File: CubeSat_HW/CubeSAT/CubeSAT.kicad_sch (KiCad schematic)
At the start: 12 parts, among them J1 Conn_02x06_Odd_Even, J2 Conn_02x04_Odd_Even, J4 Conn_01x08_Pin, J5 Conn_01x06_Pin

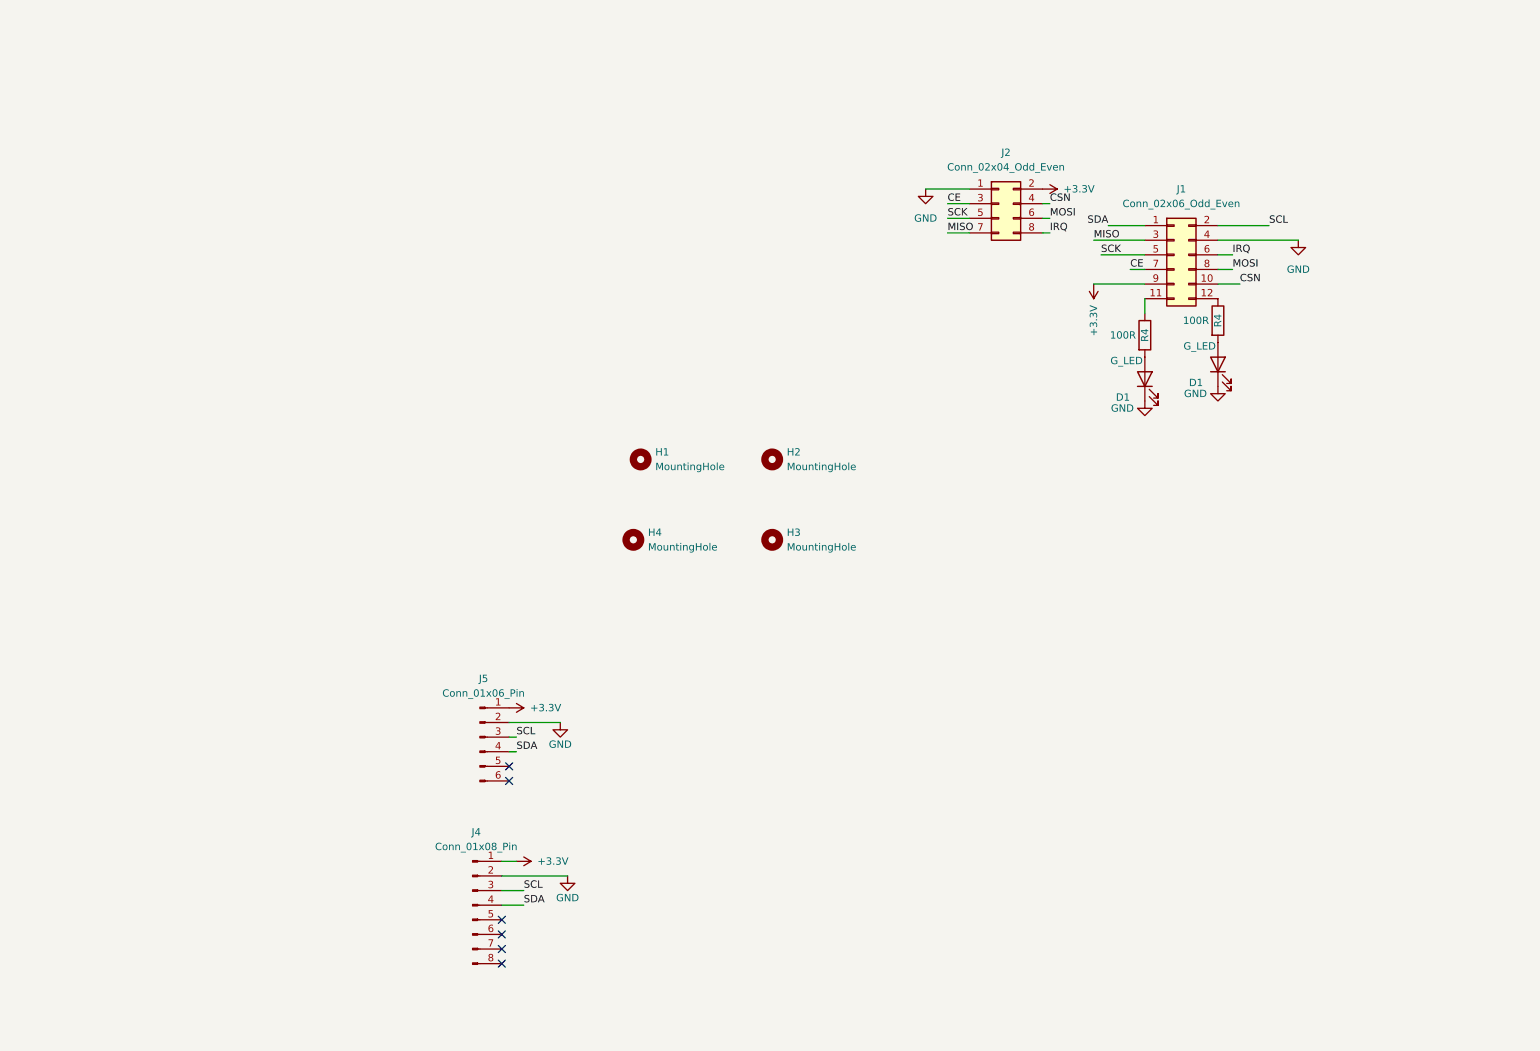
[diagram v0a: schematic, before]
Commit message: Added version 2 of the PCB
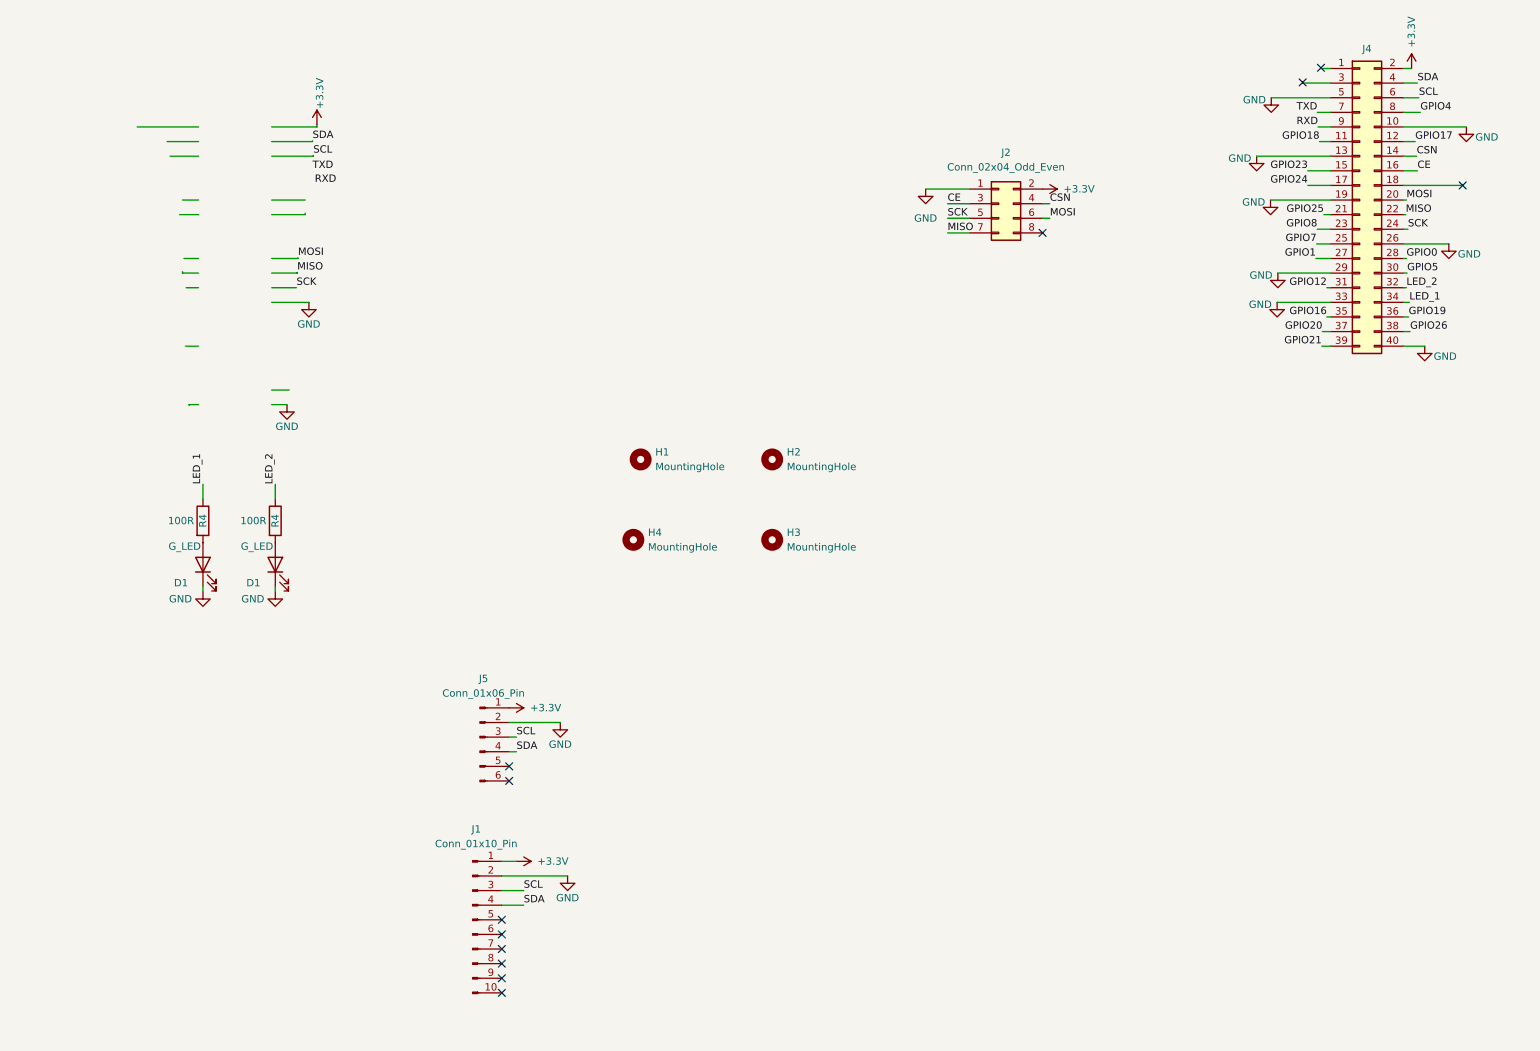
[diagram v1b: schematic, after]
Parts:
- removed J1: Conn_02x06_Odd_Even, Connector_IDC:IDC-Header_2x06_P2.54mm_Horizontal, symbol Connector_Generic:Conn_02x06_Odd_Even
- removed J4: Conn_01x08_Pin, Connector_PinSocket_2.54mm:PinSocket_1x08_P2.54mm_Vertical, symbol Connector:Conn_01x08_Pin
- added J1: Conn_01x10_Pin, Connector_PinHeader_2.54mm:PinHeader_1x10_P2.54mm_Vertical, symbol Connector:Conn_01x10_Pin
- added J4: Conn_02x20_Odd_Even, Connector_PinHeader_2.54mm:PinHeader_2x20_P2.54mm_Vertical, symbol Connector_Generic:Conn_02x20_Odd_Even
- H1, H2, H3, H4: footprint MountingHole:MountingHole_3.2mm_M3 -> MountingHole:MountingHole_2.7mm
- J5: footprint Connector_PinSocket_2.54mm:PinSocket_1x06_P2.54mm_Vertical -> Connector_PinHeader_2.54mm:PinHeader_1x06_P2.54mm_Vertical
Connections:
- net +3.3V: now also J1.1 (Pin_1), J4.2 (Pin_2)
- net CE: now also J4.16 (Pin_16)
- net CSN: now also J4.14 (Pin_14)
- net GND: now also J1.2 (Pin_2), J4.10 (Pin_10), J4.13 (Pin_13), J4.19 (Pin_19), J4.26 (Pin_26), J4.29 (Pin_29), J4.33 (Pin_33), J4.40 (Pin_40), J4.5 (Pin_5)
- net MISO: now also J4.22 (Pin_22)
- net MOSI: now also J4.20 (Pin_20)
- net SCK: now also J4.24 (Pin_24)
- net SCL: now also J1.3 (Pin_3), J4.6 (Pin_6)
- net SDA: now also J1.4 (Pin_4), J4.4 (Pin_4)
- net LED_1: now reaches R4.1
- net LED_1: now also J4.34 (Pin_34)
- net LED_2: now reaches R4.1
- net LED_2: now also J4.32 (Pin_32)
- net IRQ: no longer names the net of J2.8 (Pin_8)
- new net GPIO0: J4.28 (Pin_28)
- new net GPIO1: J4.27 (Pin_27)
- new net GPIO12: J4.31 (Pin_31)
- new net GPIO16: J4.35 (Pin_35)
- new net GPIO17: J4.12 (Pin_12)
- new net GPIO18: J4.11 (Pin_11)
- new net GPIO19: J4.36 (Pin_36)
- new net GPIO20: J4.37 (Pin_37)
- new net GPIO21: J4.39 (Pin_39)
- new net GPIO23: J4.15 (Pin_15)
- new net GPIO24: J4.17 (Pin_17)
- new net GPIO25: J4.21 (Pin_21)
- new net GPIO26: J4.38 (Pin_38)
- new net GPIO4: J4.8 (Pin_8)
- new net GPIO5: J4.30 (Pin_30)
- new net GPIO7: J4.25 (Pin_25)
- new net GPIO8: J4.23 (Pin_23)
- new net RXD: J4.9 (Pin_9)
- new net TXD: J4.7 (Pin_7)
- no-connect marks 6 -> 12
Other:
- moved on the sheet: D1, R4

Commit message: feat: Added Power and Com PCB
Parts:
- removed J5: Conn_01x06_Pin, Connector_PinHeader_2.54mm:PinHeader_1x06_P2.54mm_Vertical, symbol Connector:Conn_01x06_Pin
- added D1 (x3): G_LED, LED_SMD:LED_0603_1608Metric, symbol Device:LED
- added R4 (x3): 100R, Resistor_SMD:R_0603_1608Metric, symbol Device:R
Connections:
- net GND: now also D1.1 (K), D1.1 (K), D1.1 (K)
- net GPIO17 renamed LED4
- net LED4: now also R4.1
- net GPIO19 renamed LED5
- net LED5: now also R4.1
- net GPIO4 renamed LED3
- net LED3: now also R4.1
- new net: D1.2 (A), R4.2 (x3)
- no-connect marks 12 -> 10
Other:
- moved on the sheet: D1, H1, H2, H3, H4, J1, R4

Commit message: feat: Added GBR, BOM, CPL files for the project
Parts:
- removed J4: Conn_02x20_Odd_Even, Connector_PinHeader_2.54mm:PinHeader_2x20_P2.54mm_Vertical, symbol Connector_Generic:Conn_02x20_Odd_Even
- added J3: Conn_02x17_Odd_Even, Connector_IDC:IDC-Header_2x17_P2.54mm_Horizontal, symbol Connector_Generic:Conn_02x17_Odd_Even
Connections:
- net +3.3V: now also J3.1 (Pin_1), J3.2 (Pin_2)
- net CE: now also J3.17 (Pin_17), J3.18 (Pin_18)
- net CSN: now also J3.15 (Pin_15), J3.16 (Pin_16)
- net GND: now also J3.3 (Pin_3), J3.33 (Pin_33), J3.34 (Pin_34), J3.4 (Pin_4)
- net LED3: now also J3.23 (Pin_23), J3.24 (Pin_24)
- net LED4: now also J3.25 (Pin_25), J3.26 (Pin_26)
- net LED5: now also J3.27 (Pin_27), J3.28 (Pin_28)
- net LED_1: now also J3.19 (Pin_19), J3.20 (Pin_20)
- net LED_2: now also J3.21 (Pin_21), J3.22 (Pin_22)
- net MISO: now also J3.11 (Pin_11), J3.12 (Pin_12)
- net MOSI: now also J3.10 (Pin_10), J3.9 (Pin_9)
- net SCK: now also J3.13 (Pin_13), J3.14 (Pin_14)
- net SCL: now also J3.7 (Pin_7), J3.8 (Pin_8)
- net SDA: now also J3.5 (Pin_5), J3.6 (Pin_6)
- new net PWM0: J3.29 (Pin_29), J3.30 (Pin_30)
- new net PWM1: J3.31 (Pin_31), J3.32 (Pin_32)
- no-connect marks 10 -> 7

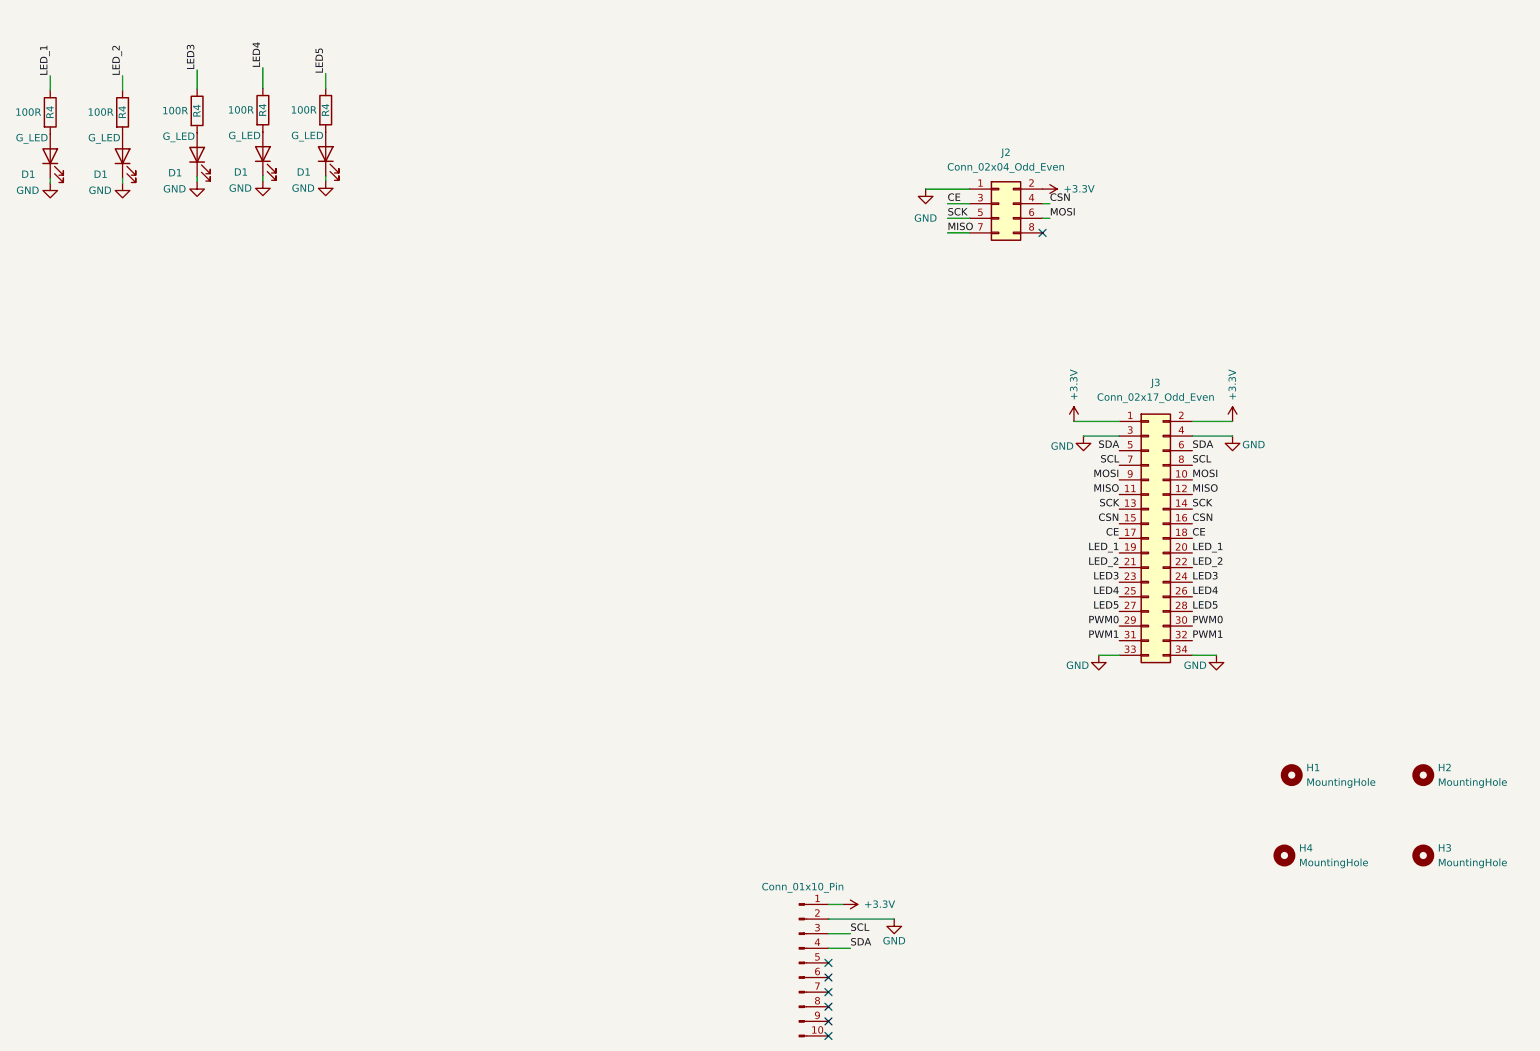
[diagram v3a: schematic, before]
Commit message: feat: Added Payload Board and new Gerbers for the project
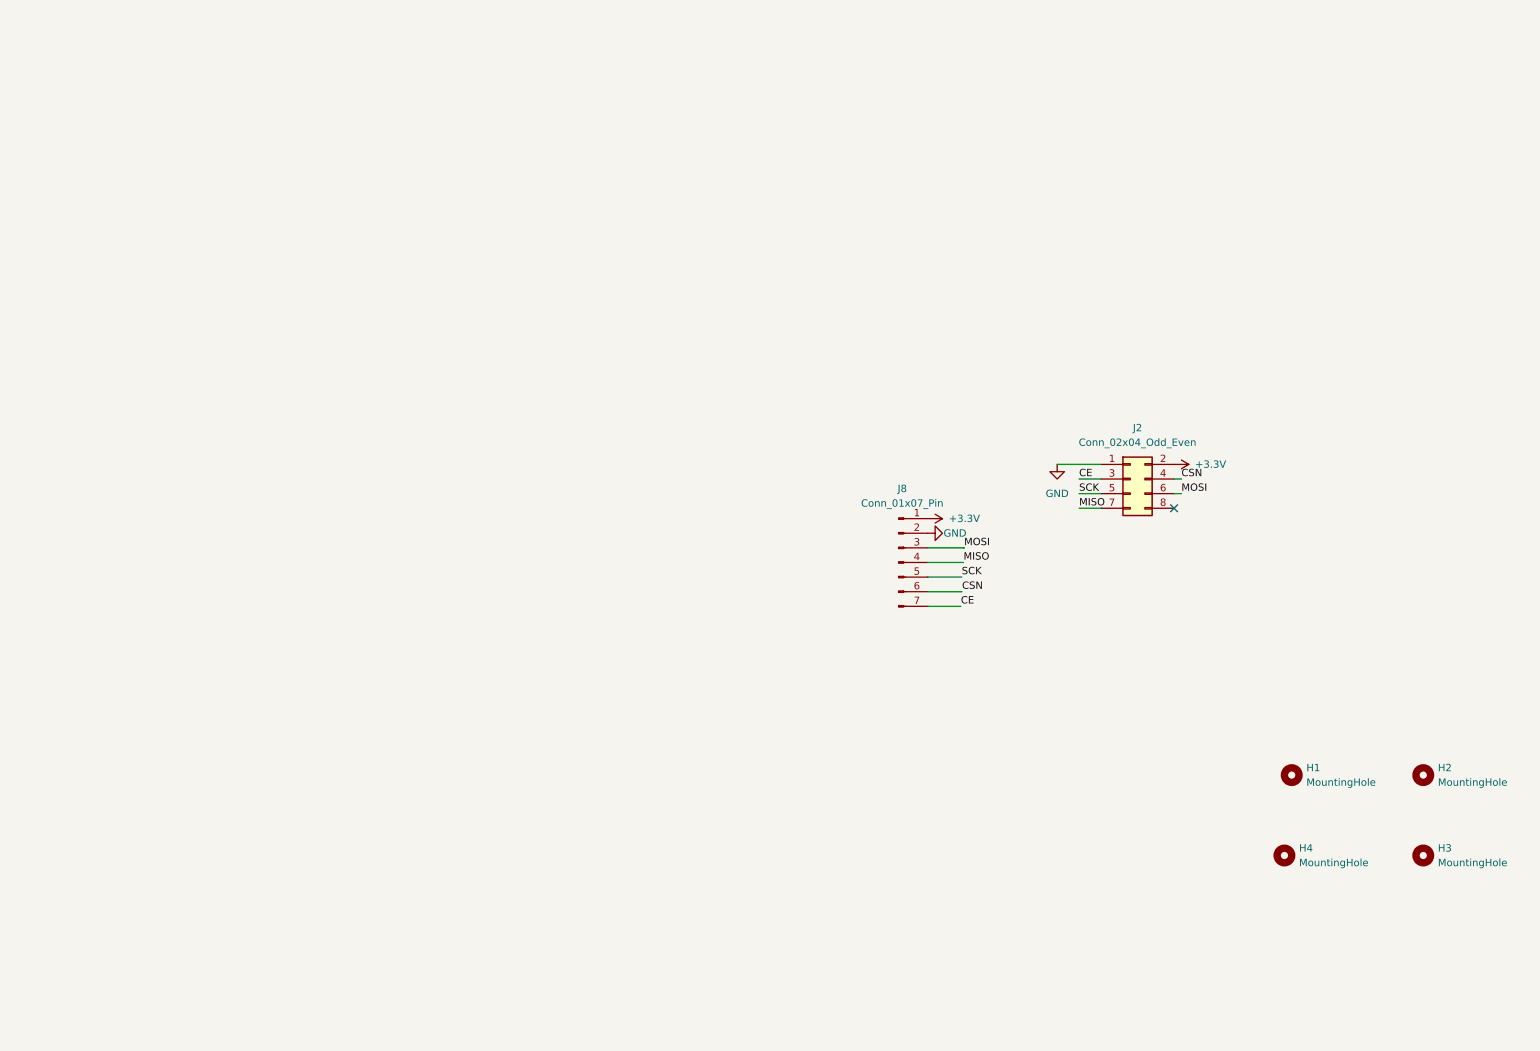
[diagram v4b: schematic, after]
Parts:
- removed D1 (x5): G_LED, LED_SMD:LED_0603_1608Metric, symbol Device:LED
- removed J1: Conn_01x10_Pin, Connector_PinHeader_2.54mm:PinHeader_1x10_P2.54mm_Vertical, symbol Connector:Conn_01x10_Pin
- removed J3: Conn_02x17_Odd_Even, Connector_IDC:IDC-Header_2x17_P2.54mm_Horizontal, symbol Connector_Generic:Conn_02x17_Odd_Even
- removed R4 (x5): 100R, Resistor_SMD:R_0603_1608Metric, symbol Device:R
- added J8: Conn_01x07_Pin, Connector_PinHeader_2.54mm:PinHeader_1x07_P2.54mm_Horizontal, symbol Connector:Conn_01x07_Pin
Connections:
- net +3.3V: now also J8.1 (Pin_1)
- net CE: now also J8.7 (Pin_7)
- net CSN: now also J8.6 (Pin_6)
- net GND: now also J8.2 (Pin_2)
- net MISO: now also J8.4 (Pin_4)
- net MOSI: now also J8.3 (Pin_3)
- net SCK: now also J8.5 (Pin_5)
- no-connect marks 7 -> 1
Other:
- moved on the sheet: J2
